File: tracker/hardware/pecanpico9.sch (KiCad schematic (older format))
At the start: 112 parts, among them IC1 SPV1040T, IC2 TPS62260DRVR, IC3 ADP322ACPZ-115-R7, IC4 Si4063-B1B-FM, IC5 STM32F413xG, IC6 EVA-7M, IC7 PAC1720-1-AIA-TR, IC8 LDLN015PU33R, IC9 BME280, P1 CONN_01X25, P2 CONN_01X10, P3 ZX62-B-5PA(33), P4 IPX 2mm, P5 CONN_01X02, P6 IPX 2mm, Q1 FDN306P, X1 KT2016K26000BCW18ZAS

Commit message: Fixed SOT-23 footprint (wrong numbering) Moved LEDs (so they are not too close to the very big inductor) Added Pulldown to GPS_EN
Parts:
- removed R13: N/A, stm32f7:R_0402, symbol R
- added R9: 100k, stm32f7:R_0402, symbol R
- C25, C27: value 470p -> 3.3p
- Q1: footprint TO_SOT_Packages_SMD:SOT-23 -> stm32f7:SOT-23
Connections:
- net +3V3: now also D2.2 (A), D3.2 (A); no longer R10.1, R11.1
- net CAM_EN: now also IC5.37 (PC6); no longer IC5.35 (PB14)
- net GND: now also R9.2
- net GPS_EN: now also R9.1
- net IO_LED2: now also IC5.33 (PB12), R10.2; no longer D2.1 (K), IC5.34 (PB13)
- net IO_LED3: now also R11.2; no longer D3.1 (K)
- new net: D2.1 (K), R10.1
- new net: D3.1 (K), R11.1
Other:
- moved on the sheet: D2, D3, R10, R11
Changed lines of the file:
@@
 	0    -1   -1   0
 $EndComp
-Text Label 19200 6100 2    60   ~ 0
+Text Label 19200 6000 2    60   ~ 0
 IO_LED2
 Text Label 19200 7350 2    60   ~ 0
@@
 L R R10
 U 1 1 57A50B73
-P 20400 6100
-F 0 "R10" V 20480 6100 50  0000 C CNN
-F 1 "1k5" V 20400 6100 50  0000 C CNN
-F 2 "stm32f7:R_0402" V 20330 6100 50  0001 C CNN
-F 3 "" H 20400 6100 50  0000 C CNN
-F 4 "1%" H 20400 6100 60  0001 C CNN "Specs"
-	1    20400 6100
+P 19900 6000
+F 0 "R10" V 19980 6000 50  0000 C CNN
+F 1 "1k5" V 19900 6000 50  0000 C CNN
+F 2 "stm32f7:R_0402" V 19830 6000 50  0001 C CNN
+F 3 "" H 19900 6000 50  0000 C CNN
+F 4 "1%" H 19900 6000 60  0001 C CNN "Specs"
+	1    19900 6000
 	0    1    1    0
 $EndComp
@@
 L R R11
 U 1 1 57A50BD6
-P 20400 7350
-F 0 "R11" V 20480 7350 50  0000 C CNN
-F 1 "1k5" V 20400 7350 50  0000 C CNN
-F 2 "stm32f7:R_0402" V 20330 7350 50  0001 C CNN
-F 3 "" H 20400 7350 50  0000 C CNN
-F 4 "1%" H 20400 7350 60  0001 C CNN "Specs"
-	1    20400 7350
+P 19900 7350
+F 0 "R11" V 19980 7350 50  0000 C CNN
+F 1 "1k5" V 19900 7350 50  0000 C CNN
+F 2 "stm32f7:R_0402" V 19830 7350 50  0001 C CNN
+F 3 "" H 19900 7350 50  0000 C CNN
+F 4 "1%" H 19900 7350 60  0001 C CNN "Specs"
+	1    19900 7350
 	0    1    1    0
 $EndComp
@@
 L LED D2
 U 1 1 57A516B3
-P 19950 6100
-F 0 "D2" H 19850 6200 50  0000 C CNN
-F 1 "blue" H 20050 6200 50  0000 C CNN
-F 2 "stm32f7:LED_0603" H 19950 6100 50  0001 C CNN
-F 3 "" H 19950 6100 50  0000 C CNN
-	1    19950 6100
+P 20350 6000
+F 0 "D2" H 20250 6100 50  0000 C CNN
+F 1 "blue" H 20450 6100 50  0000 C CNN
+F 2 "stm32f7:LED_0603" H 20350 6000 50  0001 C CNN
+F 3 "" H 20350 6000 50  0000 C CNN
+	1    20350 6000
 	1    0    0    -1
 $EndComp
@@
 L LED D3
 U 1 1 57A51790
-P 19950 7350
-F 0 "D3" H 19850 7450 50  0000 C CNN
-F 1 "green" H 20050 7450 50  0000 C CNN
-F 2 "stm32f7:LED_0603" H 19950 7350 50  0001 C CNN
-F 3 "" H 19950 7350 50  0000 C CNN
-	1    19950 7350
+P 20350 7350
+F 0 "D3" H 20250 7450 50  0000 C CNN
+F 1 "green" H 20450 7450 50  0000 C CNN
+F 2 "stm32f7:LED_0603" H 20350 7350 50  0001 C CNN
+F 3 "" H 20350 7350 50  0000 C CNN
+	1    20350 7350
 	1    0    0    -1
 $EndComp
@@
 F 0 "Q1" H 2200 9975 50  0000 L CNN
 F 1 "FDN306P" H 2200 9900 50  0000 L CNN
-F 2 "TO_SOT_Packages_SMD:SOT-23" H 2200 9825 50  0001 L CIN
+F 2 "stm32f7:SOT-23" H 2200 9825 50  0001 L CIN
 F 3 "" H 2000 9900 50  0000 L CNN
 F 4 "512-FDN306P" H 2000 9900 60  0001 C CNN "Mouser"
@@
 L +3V3 #PWR075
 U 1 1 58C08D2C
-P 20650 6000
-F 0 "#PWR075" H 20650 5850 50  0001 C CNN
-F 1 "+3V3" H 20650 6140 50  0000 C CNN
-F 2 "" H 20650 6000 50  0000 C CNN
-F 3 "" H 20650 6000 50  0000 C CNN
-	1    20650 6000
+P 20650 5900
+F 0 "#PWR075" H 20650 5750 50  0001 C CNN
+F 1 "+3V3" H 20650 6040 50  0000 C CNN
+F 2 "" H 20650 5900 50  0000 C CNN
+F 3 "" H 20650 5900 50  0000 C CNN
+	1    20650 5900
 	1    0    0    -1
 $EndComp
@@
 P 6000 14100
 F 0 "C25" H 6025 14200 50  0000 L CNN
-F 1 "470p" H 6025 14000 50  0000 L CNN
+F 1 "3.3p" H 6025 14000 50  0000 L CNN
 F 2 "stm32f7:C_0402" H 6038 13950 50  0001 C CNN
 F 3 "" H 6000 14100 50  0000 C CNN
@@
 P 6800 14100
 F 0 "C27" H 6825 14200 50  0000 L CNN
-F 1 "470p" H 6825 14000 50  0000 L CNN
+F 1 "3.3p" H 6825 14000 50  0000 L CNN
 F 2 "stm32f7:C_0402" H 6838 13950 50  0001 C CNN
 F 3 "" H 6800 14100 50  0000 C CNN
@@
 Text Notes 1050 8750 0    60   ~ 0
 If SOL_SHORT_EN is enabled, the\ncurrent of the solar cell can be\nmeasured by the PAC1720
-$Comp
-L R R13
-U 1 1 58E3356D
-P 1700 10200
-F 0 "R13" V 1780 10200 50  0000 C CNN
-F 1 "N/A" V 1700 10200 50  0000 C CNN
-F 2 "stm32f7:R_0402" V 1630 10200 50  0001 C CNN
-F 3 "" H 1700 10200 50  0000 C CNN
-F 4 "do not assemble" H 1700 10200 60  0001 C CNN "Notes"
-	1    1700 10200
-	1    0    0    -1
-$EndComp
-$Comp
-L GND #PWR084
-U 1 1 58E33E6C
-P 1700 10450
-F 0 "#PWR084" H 1700 10200 50  0001 C CNN
-F 1 "GND" H 1700 10300 50  0000 C CNN
-F 2 "" H 1700 10450 50  0000 C CNN
-F 3 "" H 1700 10450 50  0000 C CNN
-	1    1700 10450
-	1    0    0    -1
-$EndComp
 Text Label 19200 7650 2    60   ~ 0
 RADIO_GPIO1
@@
 $EndComp
 $Comp
-L GND #PWR085
+L GND #PWR084
 U 1 1 58F37956
 P 16200 4700
-F 0 "#PWR085" H 16200 4450 50  0001 C CNN
+F 0 "#PWR084" H 16200 4450 50  0001 C CNN
 F 1 "GND" H 16200 4550 50  0000 C CNN
 F 2 "" H 16200 4700 50  0000 C CNN
@@
 $EndComp
 $Comp
-L GND #PWR086
+L GND #PWR085
 U 1 1 58F3BCD7
 P 14450 3650
-F 0 "#PWR086" H 14450 3400 50  0001 C CNN
+F 0 "#PWR085" H 14450 3400 50  0001 C CNN
 F 1 "GND" H 14450 3500 50  0000 C CNN
 F 2 "" H 14450 3650 50  0000 C CNN
@@
 $EndComp
 $Comp
-L GND #PWR087
+L GND #PWR086
 U 1 1 58F3C198
 P 14650 3650
-F 0 "#PWR087" H 14650 3400 50  0001 C CNN
+F 0 "#PWR086" H 14650 3400 50  0001 C CNN
 F 1 "GND" H 14650 3500 50  0000 C CNN
 F 2 "" H 14650 3650 50  0000 C CNN
@@
 $EndComp
 $Comp
-L GND #PWR088
+L GND #PWR087
 U 1 1 58F3C335
 P 15250 3650
-F 0 "#PWR088" H 15250 3400 50  0001 C CNN
+F 0 "#PWR087" H 15250 3400 50  0001 C CNN
 F 1 "GND" H 15250 3500 50  0000 C CNN
 F 2 "" H 15250 3650 50  0000 C CNN
@@
 $EndComp
 $Comp
-L GND #PWR089
+L GND #PWR088
 U 1 1 58F3C4D2
 P 15500 3650
-F 0 "#PWR089" H 15500 3400 50  0001 C CNN
+F 0 "#PWR088" H 15500 3400 50  0001 C CNN
 F 1 "GND" H 15500 3500 50  0000 C CNN
 F 2 "" H 15500 3650 50  0000 C CNN
@@
 $EndComp
 $Comp
-L GND #PWR090
+L GND #PWR089
 U 1 1 58F3C66F
 P 15750 3650
-F 0 "#PWR090" H 15750 3400 50  0001 C CNN
+F 0 "#PWR089" H 15750 3400 50  0001 C CNN
 F 1 "GND" H 15750 3500 50  0000 C CNN
 F 2 "" H 15750 3650 50  0000 C CNN
@@
 $EndComp
 $Comp
-L GND #PWR091
+L GND #PWR090
 U 1 1 58F3C80C
 P 16000 3650
-F 0 "#PWR091" H 16000 3400 50  0001 C CNN
+F 0 "#PWR090" H 16000 3400 50  0001 C CNN
 F 1 "GND" H 16000 3500 50  0000 C CNN
 F 2 "" H 16000 3650 50  0000 C CNN
@@
 $EndComp
 $Comp
-L +1V8 #PWR092
+L +1V8 #PWR091
 U 1 1 58F3EACD
 P 15150 4000
-F 0 "#PWR092" H 15150 3850 50  0001 C CNN
+F 0 "#PWR091" H 15150 3850 50  0001 C CNN
 F 1 "+1V8" H 15150 4140 50  0000 C CNN
 F 2 "" H 15150 4000 50  0000 C CNN
@@
 $EndComp
 $Comp
-L GND #PWR093
+L GND #PWR092
 U 1 1 58F42F90
 P 15850 4700
-F 0 "#PWR093" H 15850 4450 50  0001 C CNN
+F 0 "#PWR092" H 15850 4450 50  0001 C CNN
 F 1 "GND" H 15850 4550 50  0000 C CNN
 F 2 "" H 15850 4700 50  0000 C CNN
@@
 $EndComp
 $Comp
-L GND #PWR094
+L GND #PWR093
 U 1 1 58F4F4C7
 P 18700 4250
-F 0 "#PWR094" H 18700 4000 50  0001 C CNN
+F 0 "#PWR093" H 18700 4000 50  0001 C CNN
 F 1 "GND" H 18700 4100 50  0000 C CNN
 F 2 "" H 18700 4250 50  0000 C CNN
@@
 $EndComp
 $Comp
-L GND #PWR095
+L GND #PWR094
 U 1 1 58F58554
 P 16300 8000
-F 0 "#PWR095" H 16300 7750 50  0001 C CNN
+F 0 "#PWR094" H 16300 7750 50  0001 C CNN
 F 1 "GND" H 16300 7850 50  0000 C CNN
 F 2 "" H 16300 8000 50  0000 C CNN
@@
 $EndComp
 $Comp
-L +1V8 #PWR096
+L +1V8 #PWR095
 U 1 1 58F6F224
 P 19800 5000
-F 0 "#PWR096" H 19800 4850 50  0001 C CNN
+F 0 "#PWR095" H 19800 4850 50  0001 C CNN
 F 1 "+1V8" H 19800 5140 50  0000 C CNN
 F 2 "" H 19800 5000 50  0000 C CNN
@@
 $EndComp
 $Comp
-L GND #PWR097
+L GND #PWR096
 U 1 1 58F46541
 P 15000 3650
-F 0 "#PWR097" H 15000 3400 50  0001 C CNN
+F 0 "#PWR096" H 15000 3400 50  0001 C CNN
 F 1 "GND" H 15000 3500 50  0000 C CNN
 F 2 "" H 15000 3650 50  0000 C CNN
@@
 	1    0    0    -1
 $EndComp
-Text Label 19200 6200 2    60   ~ 0
+Text Label 19200 7050 2    60   ~ 0
 CAM_EN
 $Comp
@@
 $EndComp
 $Comp
-L GND #PWR098
+L GND #PWR097
 U 1 1 591E7DCF
 P 13300 15000
-F 0 "#PWR098" H 13300 14750 50  0001 C CNN
+F 0 "#PWR097" H 13300 14750 50  0001 C CNN
 F 1 "GND" H 13300 14850 50  0000 C CNN
 F 2 "" H 13300 15000 50  0000 C CNN
@@
 $EndComp
 $Comp
-L GND #PWR099
+L GND #PWR098
 U 1 1 591ED6A9
 P 13300 13400
-F 0 "#PWR099" H 13300 13150 50  0001 C CNN
+F 0 "#PWR098" H 13300 13150 50  0001 C CNN
 F 1 "GND" H 13300 13250 50  0000 C CNN
 F 2 "" H 13300 13400 50  0000 C CNN
@@
 $EndComp
 $Comp
-L GND #PWR0100
+L GND #PWR099
 U 1 1 591F0530
 P 13300 14100
-F 0 "#PWR0100" H 13300 13850 50  0001 C CNN
+F 0 "#PWR099" H 13300 13850 50  0001 C CNN
 F 1 "GND" H 13300 13950 50  0000 C CNN
 F 2 "" H 13300 14100 50  0000 C CNN
@@
 	8900 9600 8900 9550
 Wire Wire Line
-	18600 6100 19750 6100
+	18600 6000 19750 6000
 Wire Wire Line
 	19200 7250 18600 7250
@@
 Wire Wire Line
 	1700 9250 1700 9150
-Connection ~ 1700 9950
-Wire Wire Line
-	1700 9550 1700 10050
 Wire Wire Line
 	1000 9950 1800 9950
 Connection ~ 2100 9600
 Wire Wire Line
-	20250 7350 20150 7350
+	20150 7350 20050 7350
 Wire Wire Line
 	13050 5900 13050 5800
@@
 	4500 3000 4500 3200
 Wire Wire Line
-	6100 3100 5300 3100
+	5300 3100 6100 3100
 Wire Wire Line
 	5400 2800 5400 3250
@@
 	17750 11200 17950 11200
 Wire Wire Line
-	1700 10450 1700 10350
-Wire Wire Line
 	18600 7650 19200 7650
 Wire Wire Line
@@
 	20650 7350 20550 7350
 Wire Wire Line
-	20550 6100 20650 6100
+	20550 6000 20650 6000
 Wire Wire Line
-	20650 6100 20650 6000
+	20650 6000 20650 5900
 Wire Wire Line
-	20150 6100 20250 6100
+	20050 6000 20150 6000
 Wire Wire Line
 	6950 6950 7100 6950
@@
 	19500 7450 19500 7250
 Wire Wire Line
-	19200 6200 18600 6200
+	19200 7050 18600 7050
 Wire Wire Line
 	21250 13600 21250 14350
@@
 Wire Wire Line
 	1800 4000 1800 4100
+$Comp
+L R R9
+U 1 1 5941F6B6
+P 5700 3350
+F 0 "R9" V 5780 3350 50  0000 C CNN
+F 1 "100k" V 5700 3350 50  0000 C CNN
+F 2 "stm32f7:R_0402" V 5630 3350 50  0001 C CNN
+F 3 "" H 5700 3350 50  0000 C CNN
+F 4 "1%" H 5700 3350 60  0001 C CNN "Specs"
+	1    5700 3350
+	1    0    0    -1
+$EndComp
+Wire Wire Line
+	5700 3200 5700 3100
+Connection ~ 5700 3100
+$Comp
+L GND #PWR0100
+U 1 1 59420192
+P 5700 3600
+F 0 "#PWR0100" H 5700 3350 50  0001 C CNN
+F 1 "GND" H 5700 3450 50  0000 C CNN
+F 2 "" H 5700 3600 50  0000 C CNN
+F 3 "" H 5700 3600 50  0000 C CNN
+	1    5700 3600
+	1    0    0    -1
+$EndComp
+Wire Wire Line
+	5700 3600 5700 3500
+Connection ~ 1700 9950
+Wire Wire Line
+	1700 9950 1700 9550
 $EndSCHEMATC

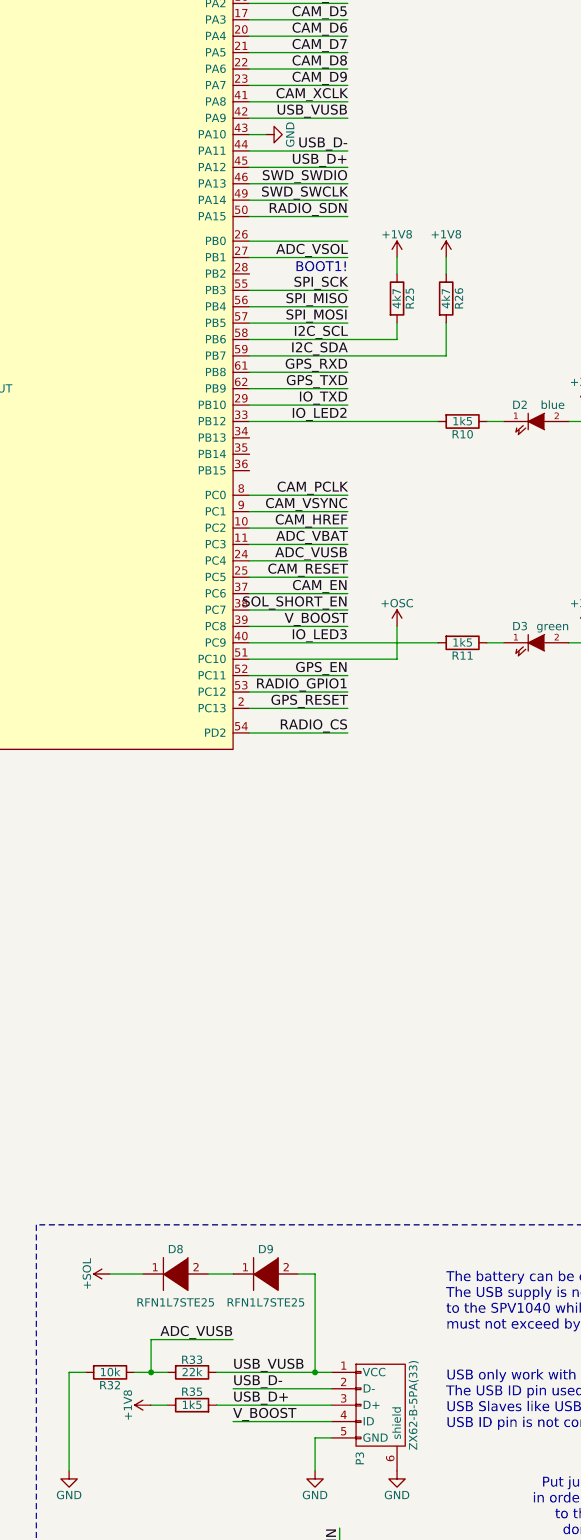
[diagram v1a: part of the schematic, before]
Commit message: Changed USB implementation
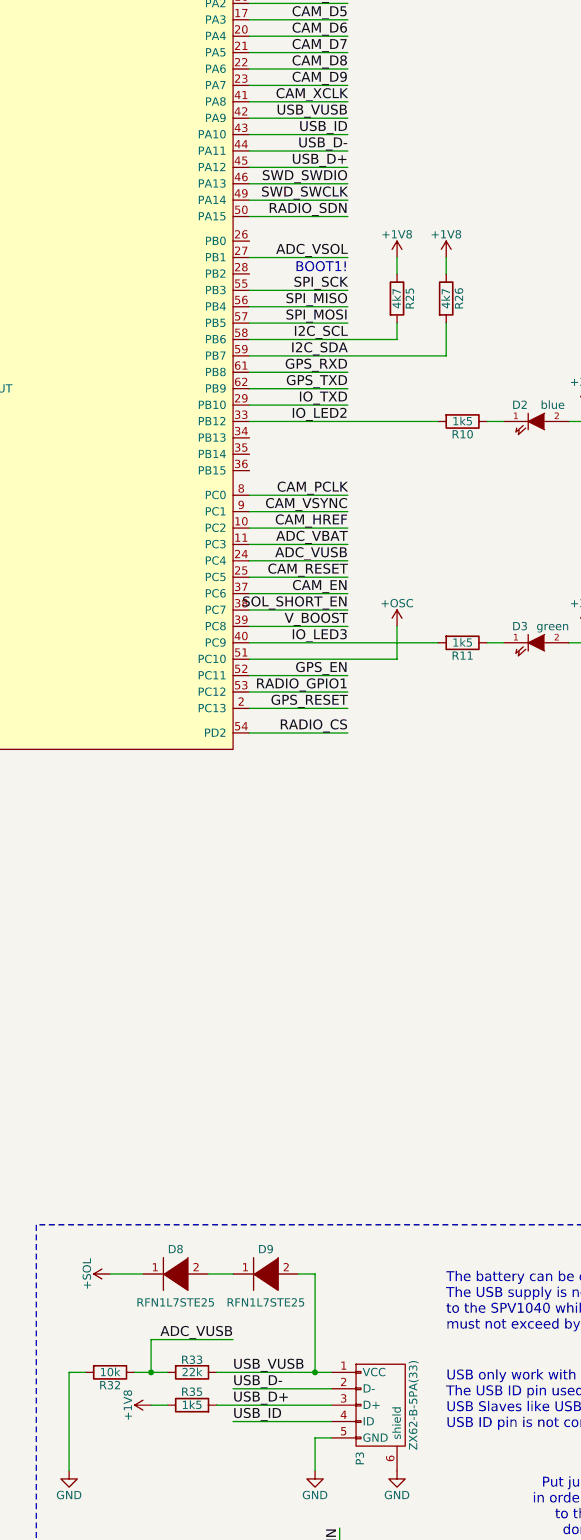
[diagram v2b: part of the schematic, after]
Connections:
- net GND: no longer IC5.43 (PA10)
- net V_BOOST: no longer P3.4 (ID)
- new net USB_ID: IC5.43 (PA10), P3.4 (ID)
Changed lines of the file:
@@
 $EndComp
 Text Label 18500 12100 0    60   ~ 0
-V_BOOST
+USB_ID
 $Comp
 L +1V8 #PWR061
@@
 $EndComp
 $Comp
-L GND #PWR093
-U 1 1 58F4F4C7
-P 18700 4250
-F 0 "#PWR093" H 18700 4000 50  0001 C CNN
-F 1 "GND" H 18700 4100 50  0000 C CNN
-F 2 "" H 18700 4250 50  0000 C CNN
-F 3 "" H 18700 4250 50  0000 C CNN
-	1    18700 4250
-	0    -1   -1   0
-$EndComp
-$Comp
 L GND #PWR094
 U 1 1 58F58554
@@
 	18600 7750 19200 7750
 Wire Wire Line
-	19200 4900 18600 4900
-Wire Wire Line
 	11900 14500 13400 14500
 Wire Wire Line
@@
 	15850 4100 16400 4100
 Wire Wire Line
-	18600 4250 18700 4250
+	18600 4250 19200 4250
 Wire Wire Line
 	12800 6500 13500 6500
@@
 Wire Wire Line
 	1700 9950 1700 9550
+Text Label 19200 4250 2    60   ~ 0
+USB_ID
 $EndSCHEMATC

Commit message: Removed OSC+ net and salvaging pin for Si4464 Changed a lot of STM32 connections
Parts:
- removed R27: 0R, stm32f7:R_0402, symbol R
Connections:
- net +1V8: now also C48.1, X1.4 (VCC)
- net CAM_EN: now also IC5.40 (PC9); no longer IC5.37 (PC6)
- net GPS_EN: now also IC5.53 (PC12); no longer IC5.52 (PC11)
- net IO_LED3: now also IC5.37 (PC6); no longer IC5.40 (PC9)
- net RADIO_GPIO1: now also IC5.52 (PC11); no longer IC5.53 (PC12)
- net SOL_SHORT_EN: now also IC5.39 (PC8); no longer IC5.38 (PC7)
- net V_BOOST: now also IC5.38 (PC7); no longer IC5.39 (PC8)
- net RADIO_GPIO0: now reaches IC4.9 (GPIO0)
- net RADIO_GPIO0: now also IC5.51 (PC10)
- removed net +OSC: C48.1, IC5.51 (PC10), X1.4 (VCC)
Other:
- moved on the sheet: D3, R11, R23, R24

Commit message: Removed I2C 0R resistors, removed USB diodes, Added USB ID
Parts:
- removed D8, D9: RFN1L7STE25, stm32f7:RFN1L7S, symbol DIODE
- removed Q1: FDN306P, stm32f7:SOT-23, symbol FDN306P
- removed R19, R20: N/A, stm32f7:R_0402, symbol R
- removed R28: 100k, stm32f7:R_0402, symbol R
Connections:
- net +1V8: no longer R25.1, R26.1
- net +3V3: now also R25.1, R26.1
- net +SOL: no longer C1.1, IC1.1 (VINSNS), IC1.8 (XSHUNT), L1.2
- net CAM_HREF: no longer IC5.10 (PC2)
- net CAM_PCLK: now also IC5.37 (PC6); no longer IC5.8 (PC0)
- net I2C_SCL: now also IC6.29 (SCL_SCK)
- net I2C_SDA: now also IC6.30 (SDA_CS)
- net IO_LED3: now also IC5.36 (PB15); no longer IC5.37 (PC6)
- net SENSE_SOL- renamed SENSE_SOL
- net SENSE_SOL: now also C1.1, IC1.1 (VINSNS), IC1.8 (XSHUNT), L1.2
- net SOL_SHORT_EN: no longer names the net of IC5.39 (PC8)
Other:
- note removed: "If SOL_SHORT_EN is enabled, the\ncurrent of the solar cell can be\nmeasured by the PAC1720"
- moved on the sheet: D3, R11, R18, R3, R4

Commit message: Reverted post hardware changes to produced version There was the plan to create Pecan Pico 9b, but all those changes have been put into Pecan Pico 10a.
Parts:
- added D8, D9: RFN1L7STE25, stm32f7:RFN1L7S, symbol DIODE
- added Q1: FDN306P, stm32f7:SOT-23, symbol FDN306P
- added R19, R20: N/A, stm32f7:R_0402, symbol R
- added R27: 0R, stm32f7:R_0402, symbol R
- added R28: 100k, stm32f7:R_0402, symbol R
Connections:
- net +1V8: now also R25.1, R26.1, R27.1; no longer C48.1, X1.4 (VCC)
- net +3V3: no longer R25.1, R26.1
- net +SOL: now also C1.1, IC1.1 (VINSNS), IC1.8 (XSHUNT), L1.2, D8.1 (K), R28.1
- net CAM_EN: now also IC5.37 (PC6); no longer IC5.40 (PC9)
- net CAM_HREF: now also IC5.10 (PC2)
- net CAM_PCLK: now also IC5.8 (PC0); no longer IC5.37 (PC6)
- net GND: now also IC5.43 (PA10), Q1.2 (D)
- net GPS_EN: now also IC5.52 (PC11); no longer IC5.53 (PC12)
- net I2C_SCL: now also R19.1; no longer IC6.29 (SCL_SCK)
- net I2C_SDA: now also R20.1; no longer IC6.30 (SDA_CS)
- net IO_LED3: now also IC5.40 (PC9); no longer IC5.36 (PB15)
- net RADIO_GPIO1: now also IC5.53 (PC12); no longer IC5.52 (PC11)
- net USB_VUSB: now also D9.2 (A)
- net V_BOOST: now also IC5.39 (PC8), P3.4 (ID); no longer IC5.38 (PC7)
- net RADIO_GPIO0: no longer names the net of IC4.9 (GPIO0)
- net RADIO_GPIO0: no longer IC5.51 (PC10)
- removed net SENSE_SOL: C1.1, IC1.1 (VINSNS), IC1.8 (XSHUNT), IC7.2 (SENSE1-), L1.2, R18.2
- removed net USB_ID: IC5.43 (PA10), P3.4 (ID)
- new net: IC6.29 (SCL_SCK), R19.2
- new net: IC6.30 (SDA_CS), R20.2
- new net: D8.2 (A), D9.1 (K)
- new net +OSC: C48.1, IC5.51 (PC10), R27.2, X1.4 (VCC)
- new net SENSE_SOL-: IC7.2 (SENSE1-), Q1.3 (S), R18.2
- new net SOL_SHORT_EN: IC5.38 (PC7), Q1.1 (G), R28.2
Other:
- note added: "If SOL_SHORT_EN is enabled, the\ncurrent of the solar cell can be\nmeasured by the PAC1720"
- moved on the sheet: D3, R11, R18, R23, R24, R3, R4
